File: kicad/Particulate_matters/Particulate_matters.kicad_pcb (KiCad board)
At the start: 2 copper layers, 60 x 30 mm, 4 parts, among them U1 XIAO-ESP32-S3-DIP, U2 GPS Module, U3 Fine Dust, U4 SD Card

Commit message: Updated schematic and pcb design
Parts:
- U2: value GPS Module -> ~; footprint Connector_PinHeader_2.54mm:PinHeader_1x05_P2.54mm_Horizontal -> Connector_PinSocket_2.54mm:PinSocket_1x05_P2.54mm_Vertical
- U3: value Fine Dust -> ~
- U4: value SD Card -> ~; footprint Connector_PinHeader_2.54mm:PinHeader_1x06_P2.54mm_Horizontal -> Connector_PinSocket_2.54mm:PinSocket_1x06_P2.54mm_Vertical
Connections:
- U1 pad 7: Net-(U1-U0TXD/D6/TX) -> unconnected-(U1-U0TXD/D6/TX-Pad7)
- U1 pad 8: unconnected-(U1-U0RXD/D7/RX-Pad8) -> Net-(U1-U0RXD/D7/RX)
- U2 pad 2: Net-(U1-GPIO3/D2/A2) -> Net-(U1-GPIO2/DA/A1)
- U2 pad 3: Net-(U1-GPIO2/DA/A1) -> Net-(U1-GPIO3/D2/A2)
- U4 pad 2: Net-(U1-GPIO9/D10/A10/MOSI) -> Net-(U1-GPIO8/D9/A9/MISO)
- U4 pad 4: Net-(U1-GPIO8/D9/A9/MISO) -> Net-(U1-GPIO9/D10/A10/MOSI)
- U4 pad 5: Net-(U1-U0TXD/D6/TX) -> Net-(U1-U0RXD/D7/RX)
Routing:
- net Net-(U1-U0TXD/D6/TX): track 43.1 -> 0.00 mm
- net Net-(U1-U0RXD/D7/RX): track 0.00 -> 27.4 mm
- net Net-(U1-GPIO3/D2/A2): track 34.2 -> 31.1 mm

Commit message: updated pcb
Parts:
- added U5: ~, Connector_PinSocket_2.54mm:PinSocket_1x04_P2.54mm_Vertical, F.Cu at (77.5, 91.4)
- moved U3 21.0 mm to (91.7, 100.6)
- moved U1 0.34 mm to (102.5, 66.5)
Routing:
- net Net-(U1-GPIO5/D4/I2C_SDA): track 17.3 -> 48.3 mm
- net Net-(U1-GPIO9/D5/I2C_SCL): track 26.6 -> 54.1 mm
- net VCC: track 91.9 -> 102.9 mm
- net Net-(U1-GPIO8/D9/A9/MISO): track 34.9 -> 24.2 mm
- net Net-(U1-GPIO9/D10/A10/MOSI): track 23.0 -> 28.1 mm
- net Net-(U1-GPIO7/D8/A8/SCK): track 23.9 -> 20.5 mm
- net GND: track 4.21 -> 1.82 mm
- net Net-(U1-GPIO2/DA/A1): track 36.3 -> 34.1 mm
- net Net-(U1-U0RXD/D7/RX): track 27.4 -> 28.9 mm
- net Net-(U1-GPIO3/D2/A2): track 31.1 -> 29.9 mm
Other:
- board size 60 x 30 mm -> 60 x 48.5 mm
- board text added: "Display"
- board text added: "Dustsensor"
- board text added: "ESP32-S3"
- board text added: "Gps"
- board text added: "Particulate Matters © GA Make 2025 https://gertjanassies.dev"
- board text added: "SD Card"

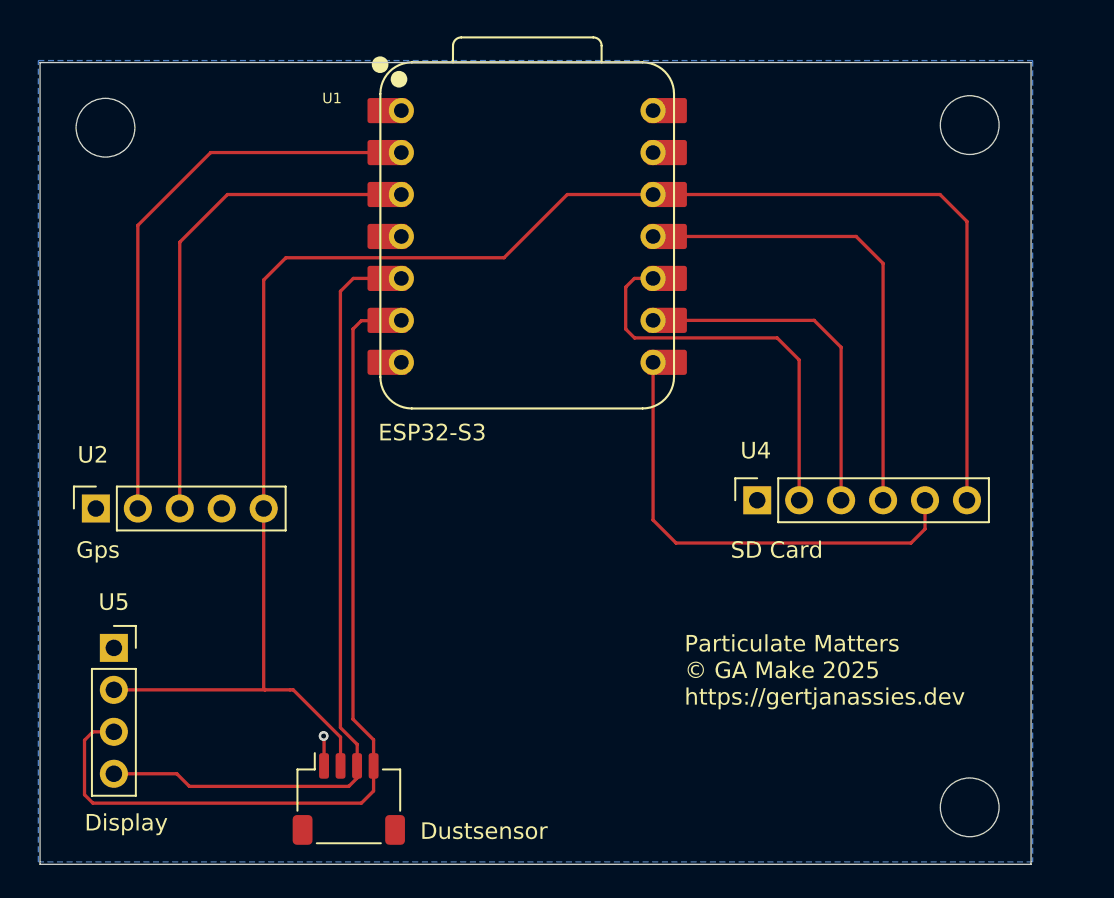
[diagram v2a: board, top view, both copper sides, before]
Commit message: AI updated version in _fixed.ino, readme now uses the svg diagram
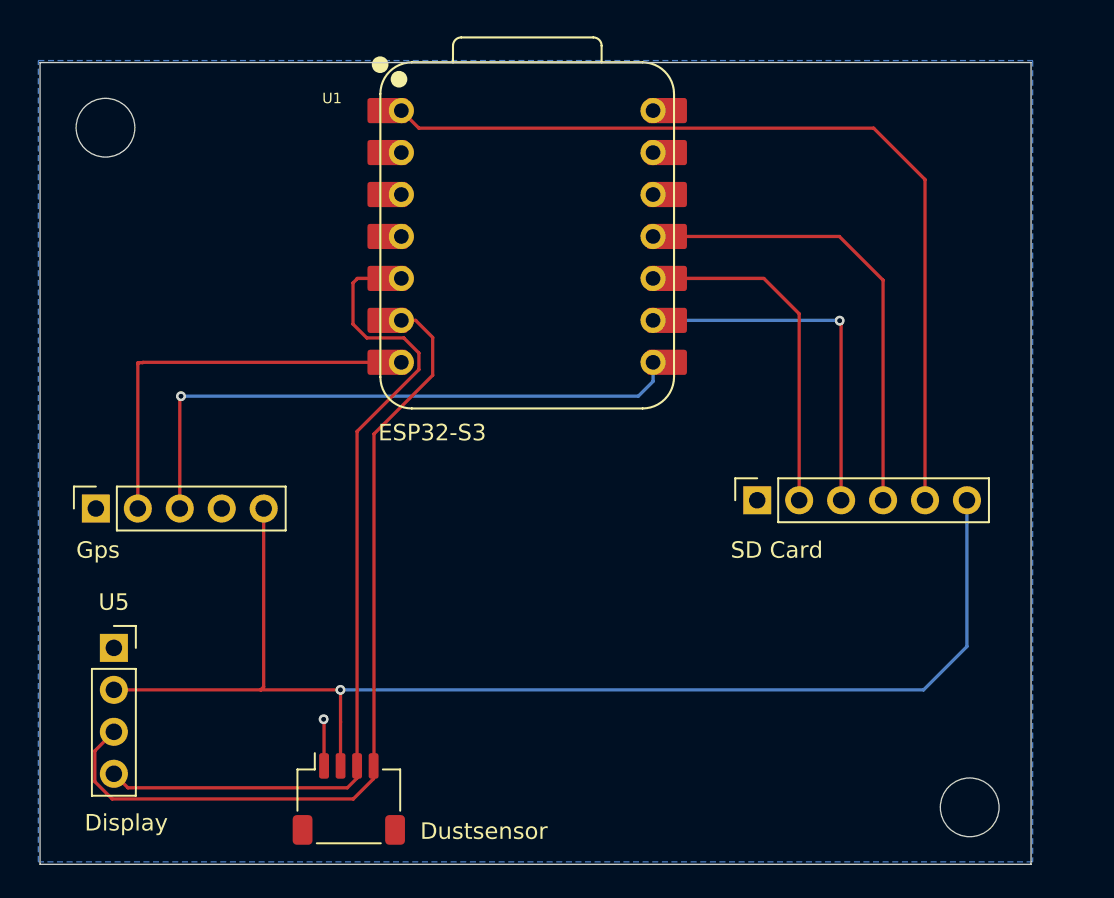
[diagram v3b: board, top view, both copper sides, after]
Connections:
- U1 pad 1: unconnected-(U1-GPIO1/D0/A0-Pad1) -> Net-(U1-GPIO1/D0/A0)
- U1 pad 2: Net-(U1-GPIO2/DA/A1) -> unconnected-(U1-GPIO2/DA/A1-Pad2)
- U1 pad 3: Net-(U1-GPIO3/D2/A2) -> unconnected-(U1-GPIO3/D2/A2-Pad3)
- U1 pad 7: unconnected-(U1-U0TXD/D6/TX-Pad7) -> Net-(U1-U0TXD/D6/TX)
- U2 pad 2: Net-(U1-GPIO2/DA/A1) -> Net-(U1-U0TXD/D6/TX)
- U2 pad 3: Net-(U1-GPIO3/D2/A2) -> Net-(U1-U0RXD/D7/RX)
- U4 pad 5: Net-(U1-U0RXD/D7/RX) -> Net-(U1-GPIO1/D0/A0)
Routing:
- net Net-(U1-GPIO1/D0/A0): track 0.00 -> 53.0 mm
- net Net-(U1-GPIO2/DA/A1): track 34.1 -> 0.00 mm
- net Net-(U1-GPIO3/D2/A2): track 29.9 -> 0.00 mm
- net VCC: track 102.9 -> 77.3 mm, vias 0 -> 1
- net Net-(U1-U0TXD/D6/TX): track 0.00 -> 24.8 mm
- net Net-(U1-U0RXD/D7/RX): track 28.9 -> 36.9 mm, vias 0 -> 1
- net Net-(U1-GPIO5/D4/I2C_SDA): track 48.3 -> 52.9 mm
- net Net-(U1-GPIO8/D9/A9/MISO): track 24.2 -> 20.2 mm
- net Net-(U1-GPIO9/D5/I2C_SCL): track 54.1 -> 51.8 mm
- net Net-(U1-GPIO7/D8/A8/SCK): track 20.5 -> 22.2 mm, vias 0 -> 1
- net GND: track 1.82 -> 2.84 mm
- net Net-(U1-GPIO9/D10/A10/MOSI): track 28.1 -> 27.5 mm
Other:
- outline, holes or cut-outs redrawn
- board text removed: "Particulate Matters © GA Make 2025 https://gertjanassies.dev"
